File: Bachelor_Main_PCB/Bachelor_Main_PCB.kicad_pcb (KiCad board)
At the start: 4 copper layers, 200 x 100 mm, 217 parts, among them IC1 LD3985M18R, J1 M20-9990245, J11 F32Q-1A7H1-11022, J13 CONMHF1-SMD-G-T, J14 CONMHF1-SMD-G-T, J2 M20-9990245, J21 CONMHF1-SMD-G-T, J25 M20-9990245, J26 691137710002, J27 Conn_01x03_Pin, J28 691137710002, J29 M20-9990245, J4 MEM2075-00-140-01-A, J8 Conn_01x07_Pin, J9 M20-9990245, P1 SF70S006VBAR2000, Q1 SSM3J358R,LF, Q10 NX3008NBKW, Q11 SSM3J358R,LF, Q12 NX3008NBKW, Q13 BC817-40Q-13-F, Q2 SSM3J358R,LF, Q3 NX3008NBKW, Q4 NX3008NBKW, Q5 NX3008NBKW, Q6 NX3008NBKW, Q7 NX3008NBKW, Q8 NX3008NBKW, Q9 NX3008NBKW, U1 USB3320C-EZK-TR, U10 LMR51450FNDRRR, U11 USB2514B-I/M2, U2 STM32H7A3ZITxQ, U3 ESD7004MUTAG, U4 ESD7004MUTAG, U5 SC0683, U6 ESD7004MUTAG, U7 RC7620_1104627, U8 LM73100RPWR, U9 LMR51450FNDRRR, Y1 ECS-327TXO-30-TR, Y2 SG-210STF 24Mhz

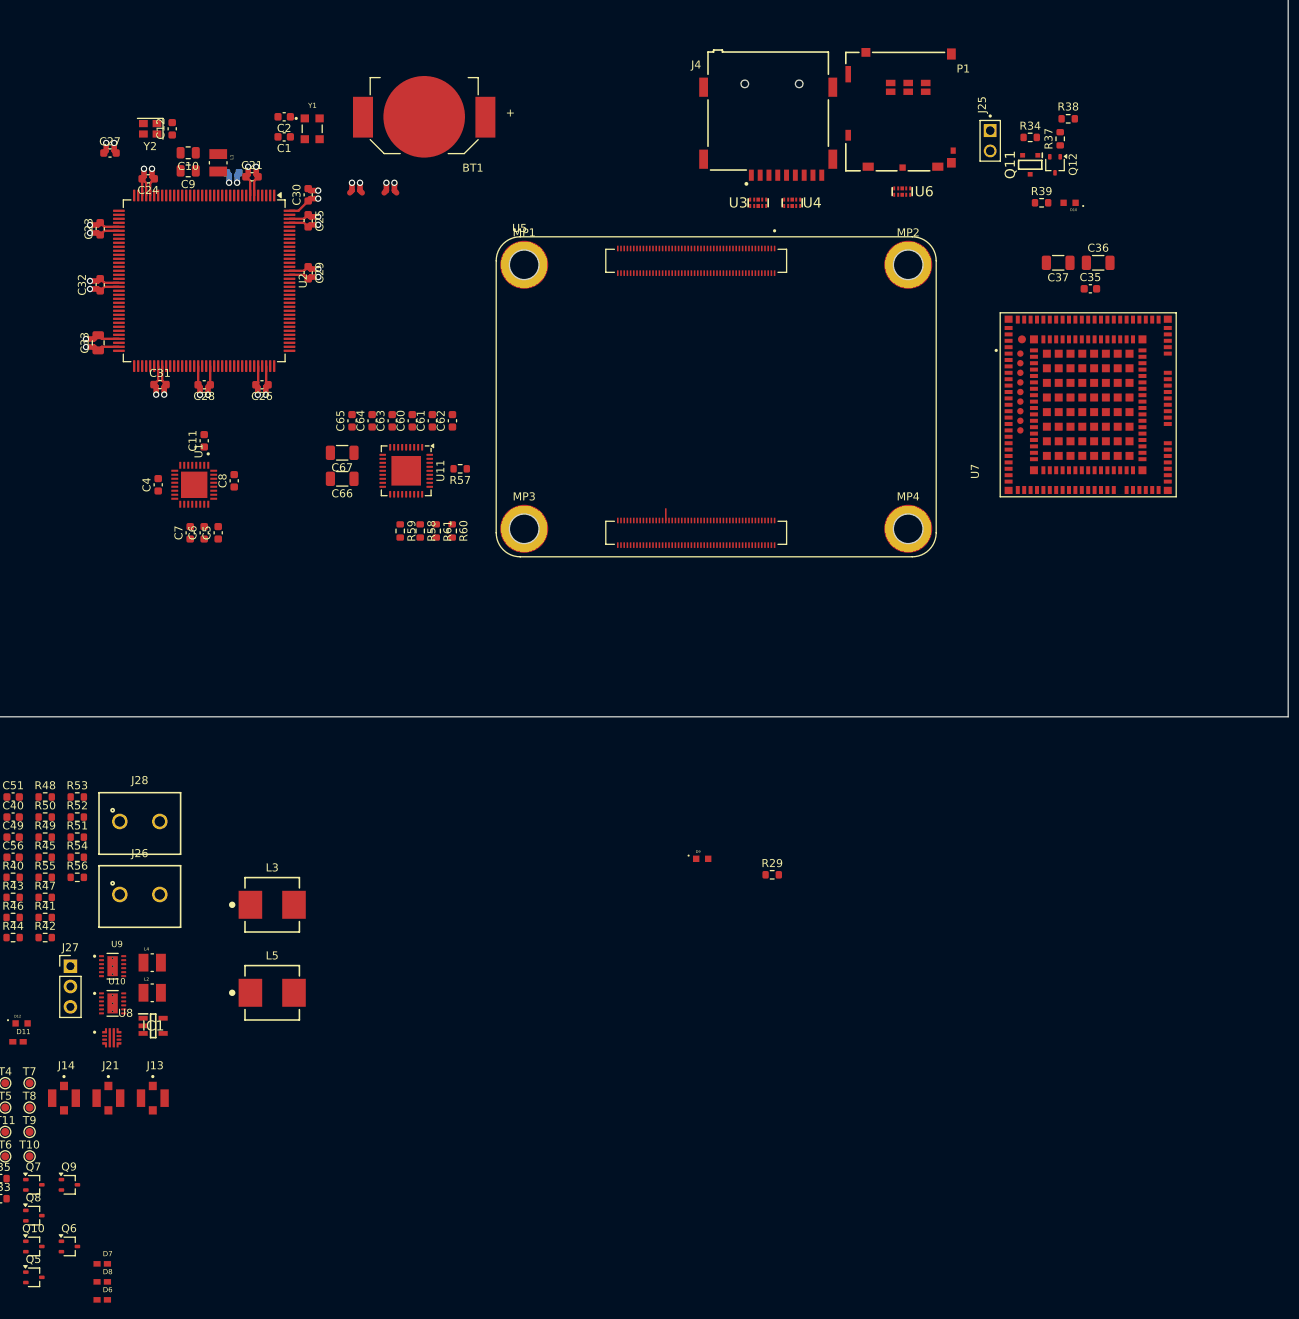
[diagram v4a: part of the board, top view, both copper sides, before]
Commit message: More arrange modem comp
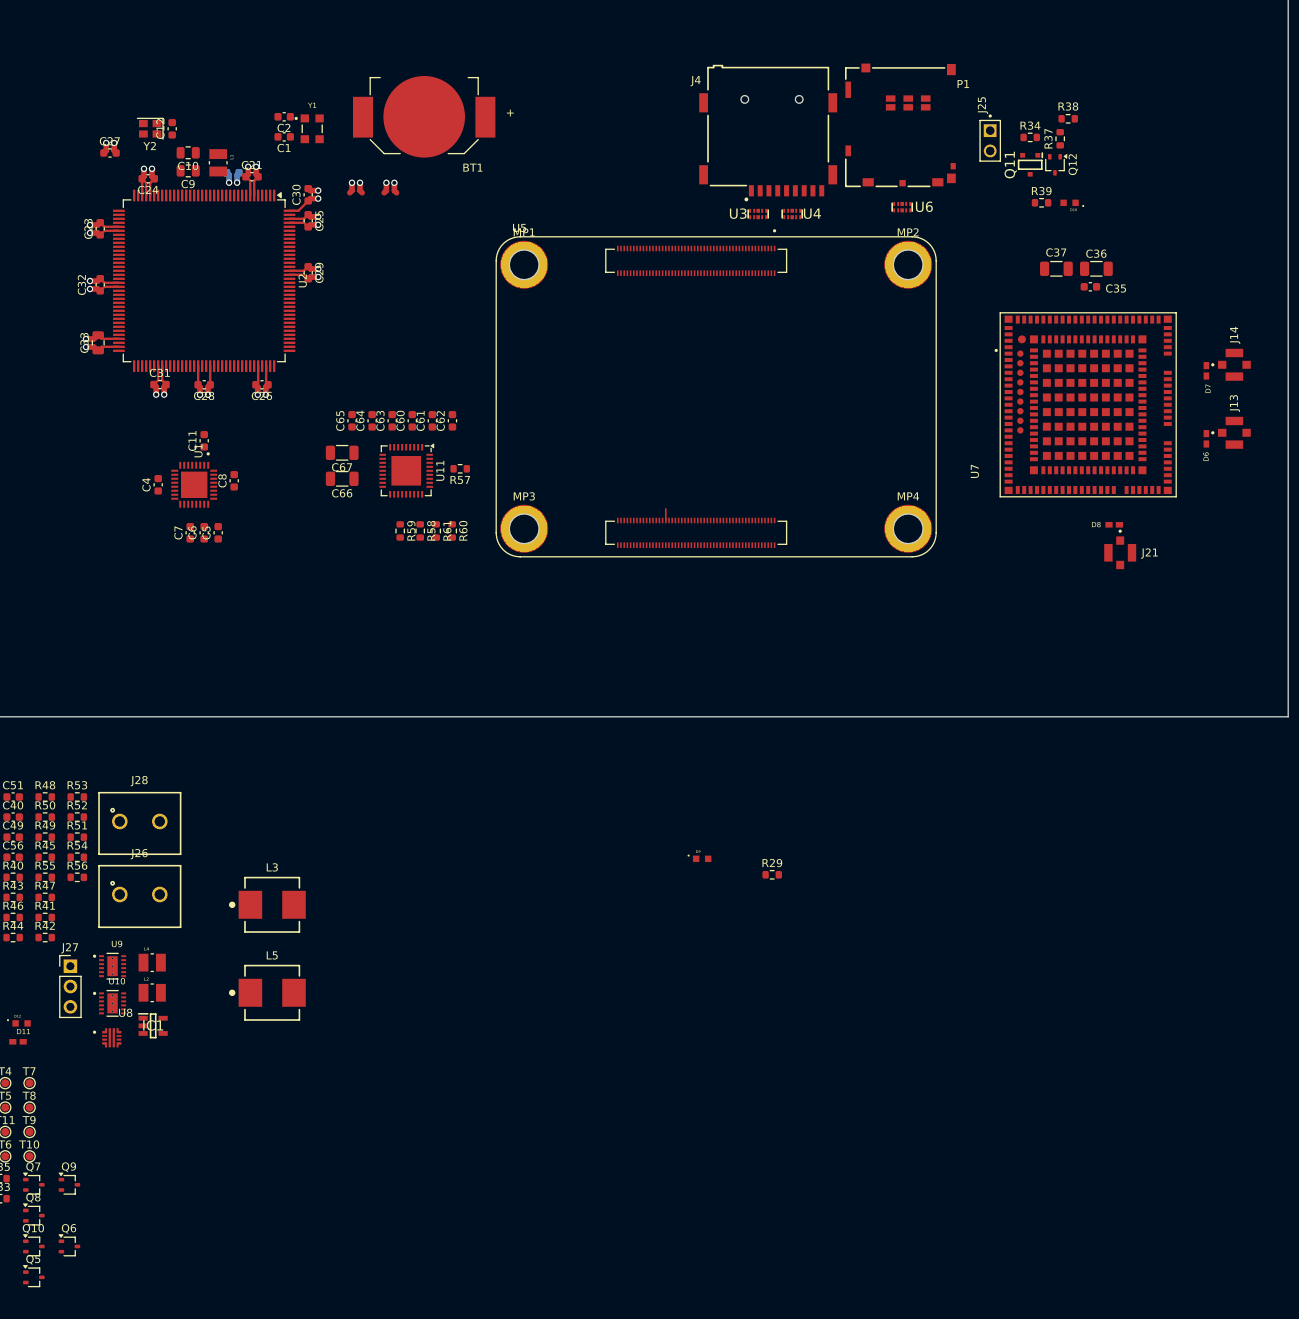
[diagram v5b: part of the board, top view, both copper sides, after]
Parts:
- moved D7 177.5 mm to (244.3, 80.8), turned to 90 degrees
- moved D6 175.0 mm to (244.3, 89.2), turned to 90 degrees
- moved J14 172.6 mm to (247.8, 80.0), turned to 90 degrees
- moved J13 158.7 mm to (247.8, 88.5), turned to 90 degrees
- moved D8 158.0 mm to (232.8, 100.0), turned to 180 degrees
- moved J21 143.7 mm to (233.5, 103.5)
- moved J4 1.95 mm to (190.0, 46.8)
- moved P1 1.95 mm to (207.0, 57.7)
- moved U6 1.95 mm to (206.2, 60.3)
- moved U3 1.40 mm to (188.2, 61.1)
- moved U4 1.40 mm to (192.5, 61.1)
- moved C36 0.78 mm to (230.5, 68.0)
- moved C37 0.78 mm to (225.5, 68.0)
- moved C35 0.25 mm to (229.8, 70.2)

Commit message: arrange Modem mosfets
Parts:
- T10, T6, T7, T8, T9: moved to B.Cu
- moved C34 187.1 mm to (214.2, 48.5), turned to 90 degrees
- moved R26 184.3 mm to (211.8, 60.0)
- moved R25 184.2 mm to (215.0, 55.8), turned to 180 degrees
- moved Q5 178.2 mm to (216.0, 60.8)
- moved T6 177.3 mm to (203.7, 39.5), turned to 90 degrees
- moved T9 174.8 mm to (206.5, 39.5), turned to 90 degrees
- moved T8 174.4 mm to (209.6, 39.5), turned to 90 degrees
- moved T7 174.1 mm to (212.6, 39.5), turned to 90 degrees
- moved T10 173.9 mm to (201.1, 39.5), turned to 90 degrees
- moved R30 172.4 mm to (213.8, 74.8)
- moved R35 169.0 mm to (215.7, 65.0)
- moved R33 167.3 mm to (215.7, 70.0), turned to 180 degrees
- moved Q9 161.8 mm to (215.9, 67.5)
- moved Q6 158.8 mm to (214.0, 77.5)
- moved R31 155.7 mm to (187.8, 74.4), turned to 90 degrees
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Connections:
- P1 pad DSW1: Net-(Q5-G) -> GND
- U3 pad 1: SDIO_D0 -> SDIO_CLK
- U3 pad 10: SDIO_D0 -> SDIO_CLK
- U3 pad 2: SDIO_D1 -> SDIO_CMD
- U3 pad 4: SDIO_D2 -> SDIO_D3
- U3 pad 5: SDIO_D3 -> SDIO_D2
- U3 pad 6: SDIO_D3 -> SDIO_D2
- U3 pad 7: SDIO_D2 -> SDIO_D3
- U3 pad 9: SDIO_D1 -> SDIO_CMD
- U4 pad 4: SDIO_CLK -> SDIO_D1
- U4 pad 5: SDIO_CMD -> SDIO_D0
- U4 pad 6: SDIO_CMD -> SDIO_D0
- U4 pad 7: SDIO_CLK -> SDIO_D1
- U6 pad 1: Net-(Q5-G) -> /Wireless modem/UIM_DATA
- U6 pad 10: Net-(Q5-G) -> /Wireless modem/UIM_DATA
- U6 pad 2: /Wireless modem/UIM_DATA -> Net-(Q5-G)
- U6 pad 9: /Wireless modem/UIM_DATA -> Net-(Q5-G)
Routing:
- net /Wireless modem/UIM_VCC: track 0.00 -> 59.6 mm, vias 0 -> 2
- net /Wireless modem/UIM_DATA: track 0.00 -> 22.7 mm
- net Net-(Q5-G): track 0.00 -> 7.29 mm
- net SDIO_CLK: track 0.00 -> 4.19 mm
- net Net-(Q11-G): track 0.00 -> 3.87 mm
- net SDIO_D1: track 0.00 -> 3.26 mm
- net SDIO_CMD: track 0.00 -> 3.14 mm
- net SDIO_D3: track 0.00 -> 3.12 mm
- net SDIO_Detect: track 0.00 -> 3.09 mm
- net SDIO_D0: track 0.00 -> 3.00 mm
- net SDIO_D2: track 0.00 -> 2.95 mm
- net /Raspberry Pi CM 4/MODEM_3V5_EN: track 0.00 -> 1.75 mm
- net Net-(Q12-G): track 0.00 -> 1.42 mm
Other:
- board size 200 x 100 mm -> 200 x 81.5 mm
- board text added: "GND here."
- board text added: "vias here"

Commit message: Add custom nettie for Waveguide. Aligned modem connectors
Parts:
- added NT1: NetTie_2, Net_tie_footprint_Waveguide_transmissionline:0.3mm_to_0.41_net_tie, F.Cu at (233.5, 96.5)
- added NT2: NetTie_2, Net_tie_footprint_Waveguide_transmissionline:0.3mm_to_0.41_net_tie, F.Cu at (240.5, 79.8)
- added NT3: NetTie_2, Net_tie_footprint_Waveguide_transmissionline:0.3mm_to_0.41_net_tie, F.Cu at (240.5, 88.6)
- moved D10 6.73 mm to (232.9, 63.2)
- moved R39 6.73 mm to (229.4, 63.2)
- moved J25 4.92 mm to (220.5, 56.0)
- moved Q11 4.92 mm to (224.2, 59.5)
- moved Q12 4.92 mm to (227.3, 59.5)
- moved R34 4.92 mm to (224.2, 56.1)
- moved R37 4.92 mm to (228.0, 56.2)
- moved R38 4.92 mm to (229.0, 53.8)
- moved D7 0.32 mm to (244.2, 80.5)
- moved J14 0.20 mm to (247.8, 79.8)
- moved D6 0.12 mm to (244.2, 89.2)
- moved D8 0.10 mm to (232.8, 100.0)
- moved J13 0.10 mm to (247.8, 88.6)
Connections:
- U7 pad 31: /Wireless modem/DIV_ANT -> Net-(U7A-RF_DIV)
- U7 pad 38: /Wireless modem/GNSS_ANT -> Net-(U7A-RF_GNSS)
- U7 pad 49: /Wireless modem/MAIN_ANT -> Net-(U7A-RF_MAIN)
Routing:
- net /Wireless modem/GNSS_ANT: track 0.00 -> 5.25 mm
- net /Wireless modem/MAIN_ANT: track 0.00 -> 5.22 mm
- net /Wireless modem/DIV_ANT: track 0.00 -> 4.92 mm
- net Net-(U7A-RF_MAIN): track 0.00 -> 3.72 mm
- net Net-(U7A-RF_GNSS): track 0.00 -> 3.72 mm
- net Net-(U7A-RF_DIV): track 0.00 -> 2.87 mm
- net /Raspberry Pi CM 4/MODEM_3V5_EN: track 1.75 -> 0.00 mm

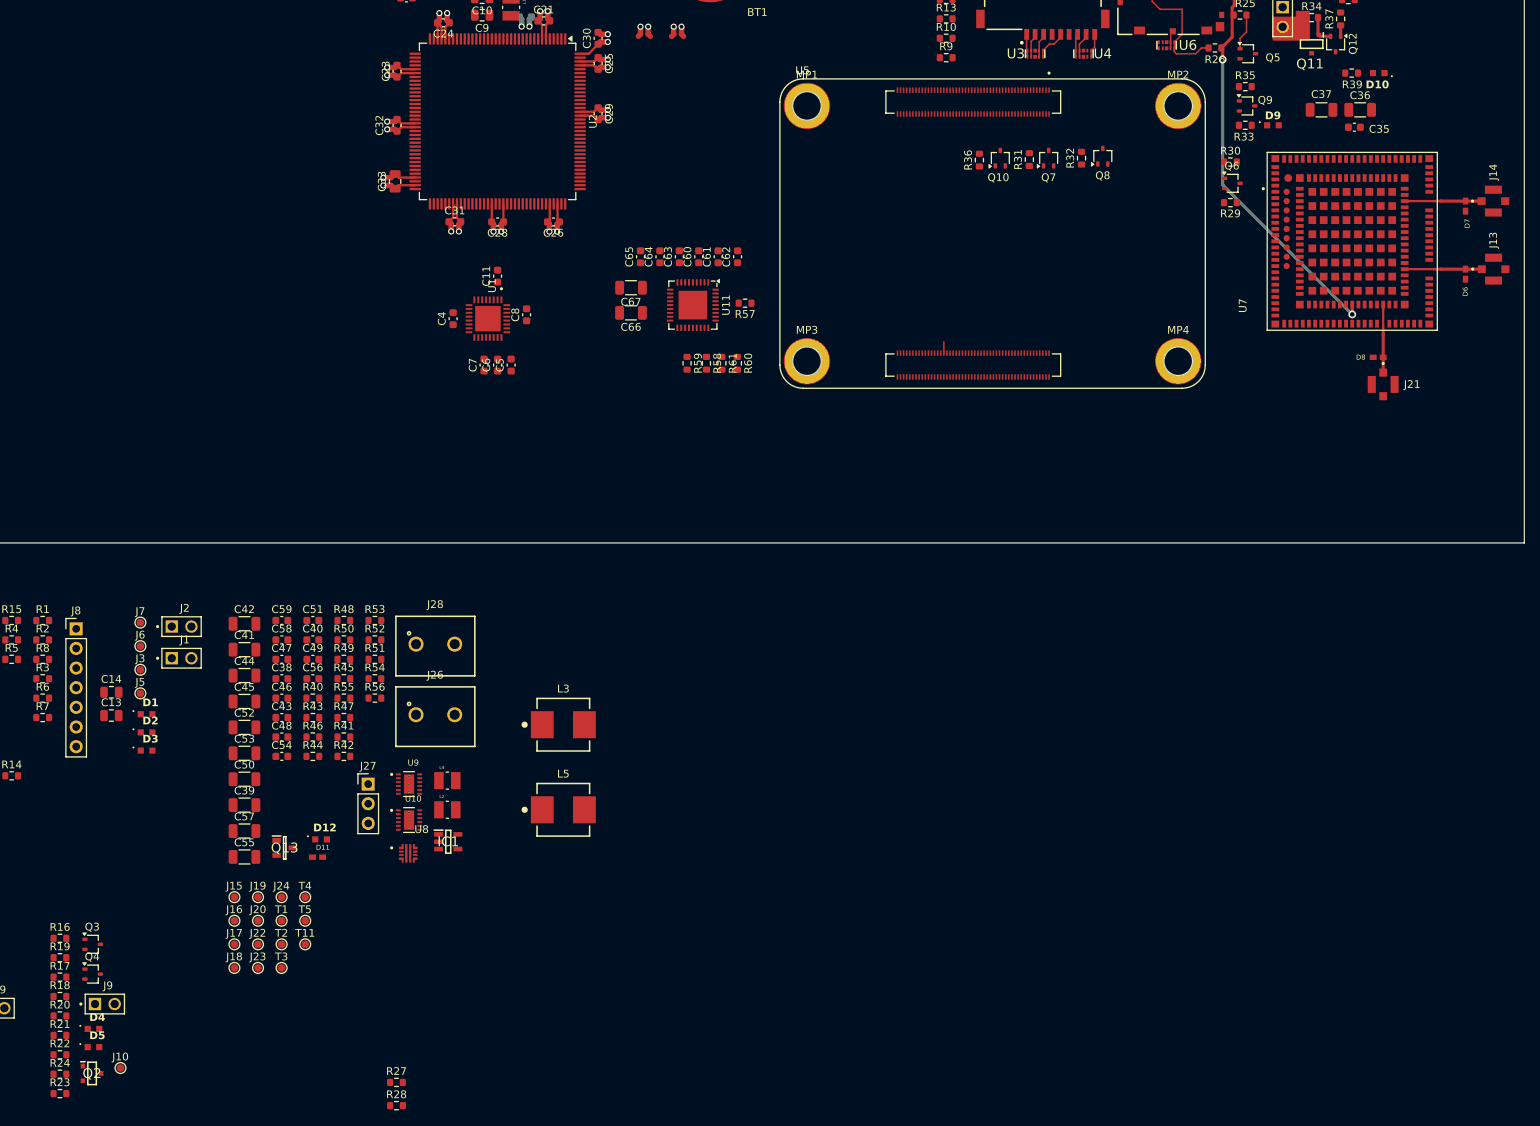
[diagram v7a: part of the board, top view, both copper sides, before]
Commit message: place modem testpoints
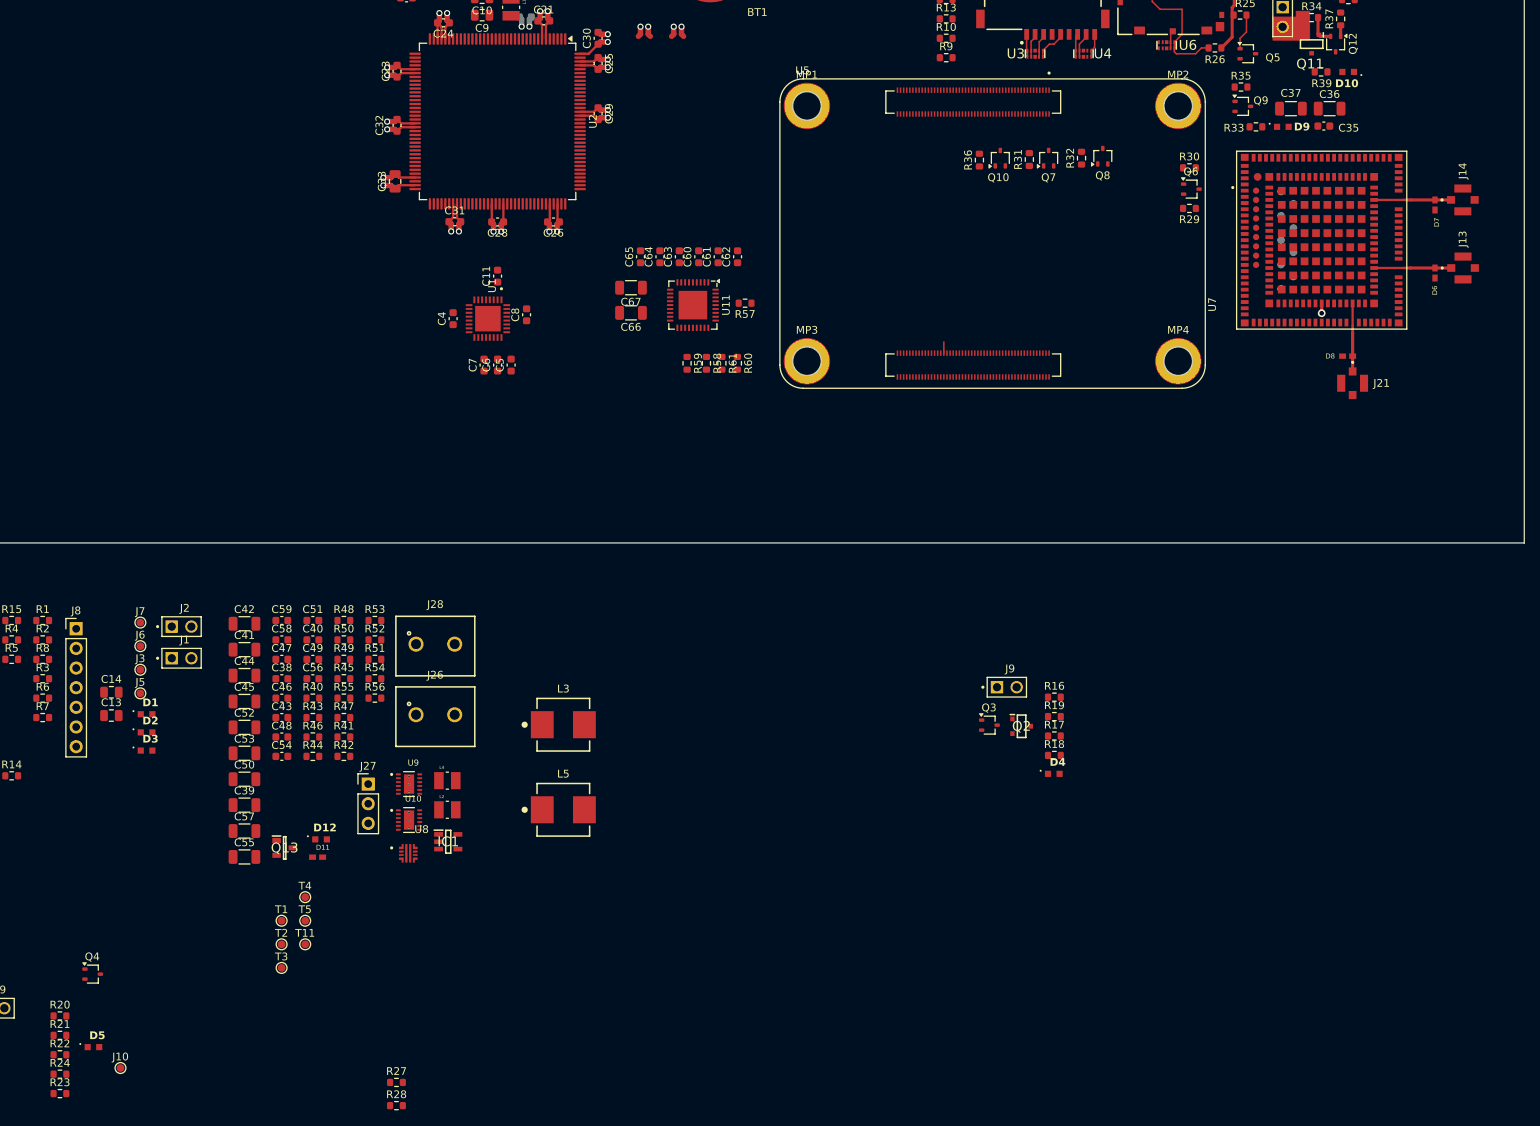
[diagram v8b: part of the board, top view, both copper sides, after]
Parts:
- J15, J16, J17, J18, J19, J20, J22, J23, J24: moved to B.Cu
- moved J18 167.0 mm to (221.9, 83.3), turned to 90 degrees
- moved J16 165.4 mm to (221.9, 80.2), turned to 90 degrees
- moved J17 164.9 mm to (220.3, 81.7), turned to -90 degrees
- moved J15 163.2 mm to (220.3, 78.5), turned to -90 degrees
- moved J23 161.0 mm to (221.9, 89.5), turned to 90 degrees
- moved J20 159.3 mm to (221.9, 86.4), turned to 90 degrees
- moved J22 158.8 mm to (220.3, 88.0), turned to -90 degrees
- moved J19 157.2 mm to (220.3, 84.8), turned to -90 degrees
- moved J24 151.3 mm to (220.3, 91.2), turned to -90 degrees
- moved R16 132.3 mm to (191.0, 143.9)
- moved R17 132.3 mm to (191.0, 149.0)
- moved R18 132.3 mm to (191.0, 151.5)
- moved R19 132.3 mm to (191.0, 146.4)
- moved D4 128.5 mm to (190.9, 153.8)
- moved Q2 128.3 mm to (186.8, 147.7)
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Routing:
- net /Wireless modem/UIM_VCC: track 59.6 -> 18.1 mm, vias 2 -> 1
